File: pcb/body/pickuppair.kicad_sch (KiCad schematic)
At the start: 23 parts, among them U2 TL072

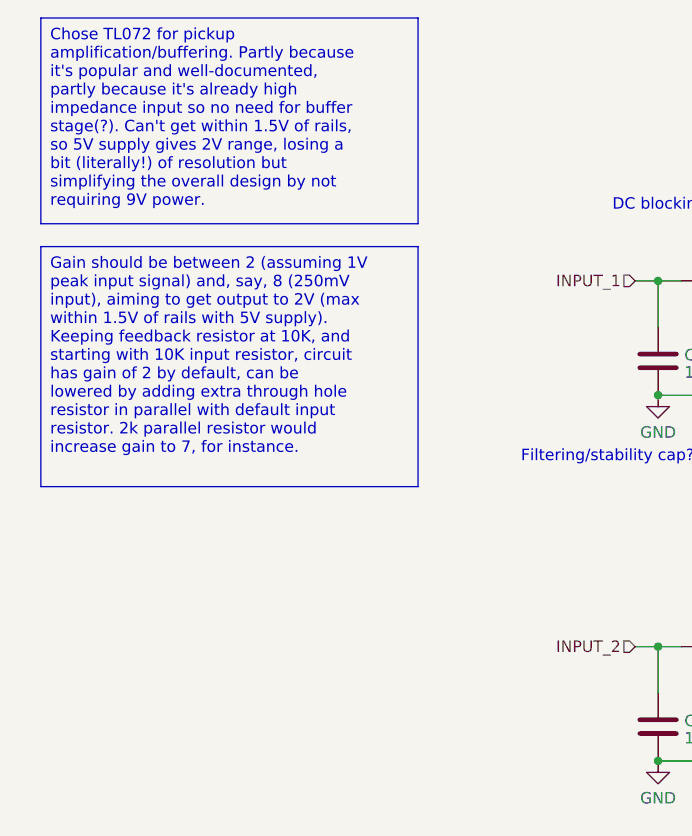
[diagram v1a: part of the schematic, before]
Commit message: linked input stages to codecs
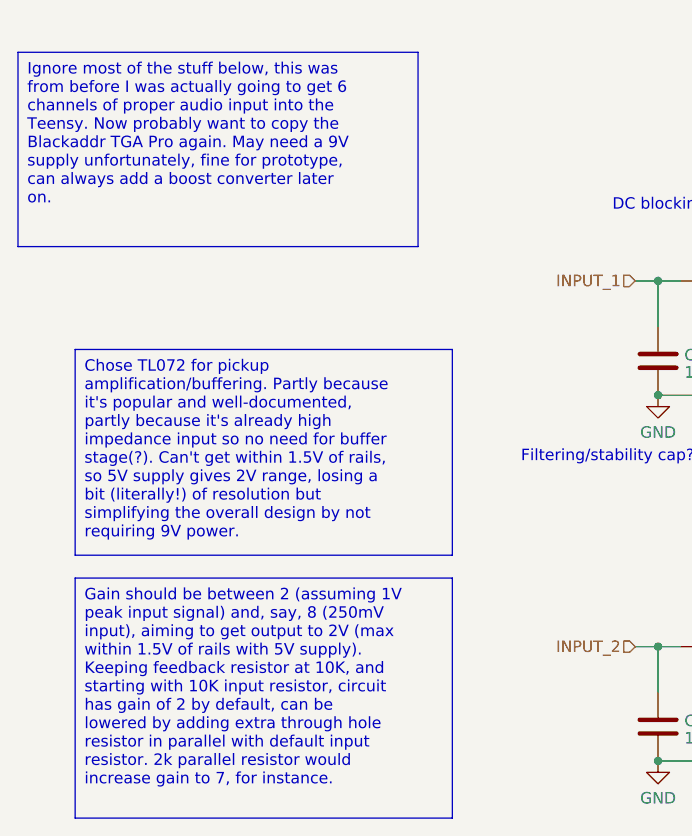
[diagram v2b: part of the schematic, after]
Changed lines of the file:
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@@
   )
   (text_box "Chose TL072 for pickup amplification/buffering. Partly because it's popular and well-documented, partly because it's already high impedance input so no need for buffer stage(?). Can't get within 1.5V of rails, so 5V supply gives 2V range, losing a bit (literally!) of resolution but simplifying the overall design by not requiring 9V power."
-    (at 20.32 13.97 0) (size 41.91 22.86)
+    (at 24.13 50.8 0) (size 41.91 22.86)
     (stroke (width 0) (type default))
     (fill (type none))
@@
   )
   (text_box "Gain should be between 2 (assuming 1V peak input signal) and, say, 8 (250mV input), aiming to get output to 2V (max within 1.5V of rails with 5V supply). Keeping feedback resistor at 10K, and starting with 10K input resistor, circuit has gain of 2 by default, can be lowered by adding extra through hole resistor in parallel with default input resistor. 2k parallel resistor would increase gain to 7, for instance."
-    (at 20.32 39.37 0) (size 41.91 26.67)
+    (at 24.13 76.2 0) (size 41.91 26.67)
     (stroke (width 0) (type default))
     (fill (type none))
+    (effects (font (size 1.27 1.27)) (justify left top))
+  )
+  (text_box "Ignore most of the stuff below, this was from before I was actually going to get 6 channels of proper audio input into the Teensy. Now probably want to copy the Blackaddr TGA Pro again. May need a 9V supply unfortunately, fine for prototype, can always add a boost converter later on."
+    (at 17.78 17.78 0) (size 44.45 21.59)
+    (stroke (width 0) (type default))
+    (fill (type none))

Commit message: nice progress
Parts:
- removed R10: 1M, symbol Device:R_US
- removed R12: 10k, symbol Device:R_US
- removed R15: 2.2k, symbol Device:R_US
- removed R16: 20k, symbol Device:R_US
- added C10, C11: 1u, Capacitor_SMD:C_0603_1608Metric, symbol Device:C
- added C7: 100n, Capacitor_SMD:C_0603_1608Metric, symbol Device:C
- added C8, C9: 1n, Capacitor_SMD:C_0603_1608Metric, symbol Device:C
- added D1, D2: BAT54S, Package_TO_SOT_SMD:SOT-23, symbol Diode:BAT54S
- C1: value 100p -> 0.1u; footprint (none) -> Capacitor_SMD:C_0603_1608Metric
- C2: value 1u -> 0.1u; footprint (none) -> Capacitor_SMD:C_0603_1608Metric
- C3: value 1n -> 10u; footprint (none) -> Capacitor_SMD:C_0603_1608Metric
- C4: value 100p -> 10u; footprint (none) -> Capacitor_SMD:C_0603_1608Metric
- C5: value 1u -> 18p; footprint (none) -> Capacitor_SMD:C_0603_1608Metric
- C6: value 1n -> 18p; footprint (none) -> Capacitor_SMD:C_0603_1608Metric
- R1: value 1k -> 1M; footprint (none) -> Resistor_SMD:R_0603_1608Metric
- R11: value 1M -> Gain; footprint (none) -> Resistor_THT:R_Axial_DIN0207_L6.3mm_D2.5mm_P2.54mm_Vertical
- R13: value 1k to 20k -> 1k; footprint Resistor_THT:R_Axial_DIN0207_L6.3mm_D2.5mm_P7.62mm_Horizontal -> Resistor_SMD:R_0603_1608Metric
- R14: value 10k -> 1k; footprint (none) -> Resistor_SMD:R_0603_1608Metric
- R2: footprint (none) -> Resistor_SMD:R_0603_1608Metric
- R3: value 1M -> 2M; footprint (none) -> Resistor_SMD:R_0603_1608Metric
- R4, R5: value 10k -> 2M; footprint (none) -> Resistor_SMD:R_0603_1608Metric
- R6: value 1k to 20k -> 2M; footprint Resistor_THT:R_Axial_DIN0207_L6.3mm_D2.5mm_P7.62mm_Horizontal -> Resistor_SMD:R_0603_1608Metric
- R7: value 20k -> 10k; footprint (none) -> Resistor_SMD:R_0603_1608Metric
- R8: value 2.2k -> 10k; footprint (none) -> Resistor_SMD:R_0603_1608Metric
- R9: value 1k -> Gain; footprint (none) -> Resistor_THT:R_Axial_DIN0207_L6.3mm_D2.5mm_P2.54mm_Vertical
- U2: footprint (none) -> Package_SO:SOIC-8_3.9x4.9mm_P1.27mm
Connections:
- net GND: now also C3.1, C4.1, R1.2, R2.2, C7.1, C8.2, C9.2, D1.1 (A), D2.1 (A); no longer C1.2, C3.2, C4.2, C6.2, R11.2, R13.2, R3.2, R7.2
- net INPUT_1: now also R1.1; no longer C2.2
- net INPUT_2: now also C2.1, R2.1; no longer C4.1, C5.2
- net OUTPUT_1: now also C10.1, D1.3 (COM); no longer R5.1, R7.1, R8.2, U2.1
- net OUTPUT_2: now also C11.1, D2.3 (COM); no longer R14.1, U2.7
- net at C5.1, R9.1: now also R7.2, U2.2 (-)
- net at C6.1, R11.1: now also R8.2, U2.6 (-); no longer R9.2, U2.5 (+)
- net at R5.2, R6.1: now also C2.2, U2.5 (+); no longer R4.1, U2.2 (-)
- removed net +5V: R2.1, R8.1, U2.8 (V+)
- new net: C4.2, R8.1
- new net: C5.2, R13.1, R9.2, U2.1
- new net: C10.2, C8.1, R13.2
- new net: C11.2, C9.1, R14.2
- new net: C6.2, R11.2, R14.1, U2.7
- new net: C3.2, R7.1
- new net: C1.2, R3.2, R4.1, U2.3 (+)
- new net +3.3V: D1.2 (K), D2.2 (K)
- new net +9V: C7.2, R3.1, R5.1, U2.8 (V+)
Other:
- note added: "Drain, prevents pop when switching to bypass"
- note removed: "Biasing input to 2.5V"
- note removed: "DC blocking cap"
- note removed: "Feedback resistor"
- note removed: "Filtering/stability cap?"
- note removed: "Impedance matching resistor?"
- note removed: "Input resistors (one fixed, another left unpopulated for adjustment)"
- note removed: "Non-inverting amplifier circuit"
